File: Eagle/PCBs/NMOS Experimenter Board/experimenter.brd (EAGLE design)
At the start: 83.8 x 99.1 mm, 1526 parts, among them Q100 2N7002, Q101 2N7002, Q102 2N7002, Q103 2N7002, Q104 2N7002, Q105 2N7002, Q106 2N7002, Q107 2N7002, Q108 2N7002, Q109 2N7002, Q110 2N7002, Q111 2N7002, Q112 2N7002, Q113 2N7002, Q114 2N7002, Q115 2N7002, Q116 2N7002, Q117 2N7002, Q118 2N7002, Q119 2N7002, Q120 2N7002, Q2 2N7002, Q25 2N7002, Q26 2N7002, Q27 2N7002, Q28 2N7002, Q29 2N7002, Q3 2N7002, Q30 2N7002, Q31 2N7002, Q32 2N7002, Q33 2N7002, Q34 2N7002, Q35 2N7002, Q36 2N7002, Q37 2N7002, Q38 2N7002, Q39 2N7002, Q4 2N7002, Q40 2N7002, Q41 2N7002, Q42 2N7002, Q43 2N7002, Q44 2N7002, Q45 2N7002, Q46 2N7002, Q47 2N7002, Q48 2N7002, Q49 2N7002, Q5 2N7002, Q50 2N7002, Q51 2N7002, Q52 2N7002, Q53 2N7002, Q54 2N7002, Q55 2N7002, Q56 2N7002, Q57 2N7002, Q58 2N7002, Q59 2N7002, Q6 2N7002, Q60 2N7002, Q61 2N7002, Q62 2N7002, Q63 2N7002, Q64 2N7002, Q65 2N7002, Q66 2N7002, Q67 2N7002, Q68 2N7002, Q69 2N7002, Q7 2N7002, Q70 2N7002, Q71 2N7002, Q72 2N7002, Q73 2N7002, Q74 2N7002, Q75 2N7002, Q76 2N7002, Q77 2N7002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

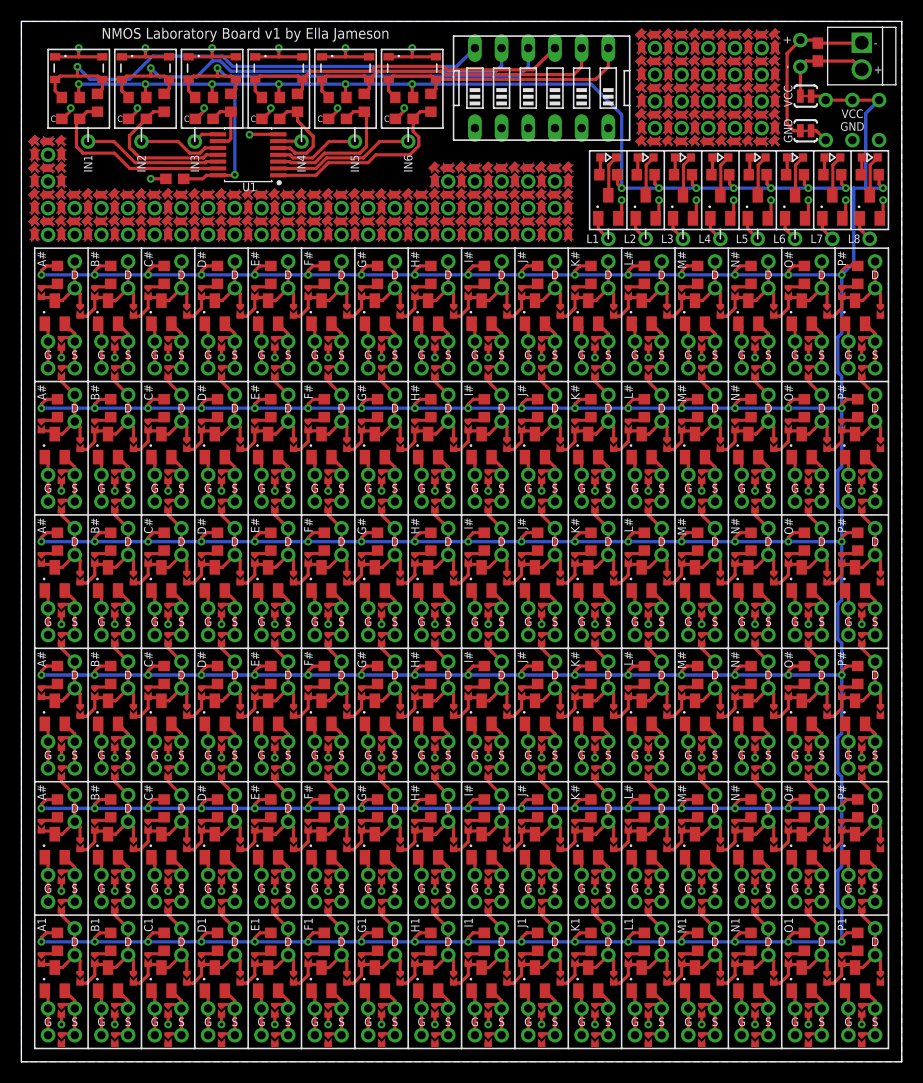
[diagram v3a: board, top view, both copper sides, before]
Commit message: Better power distribution
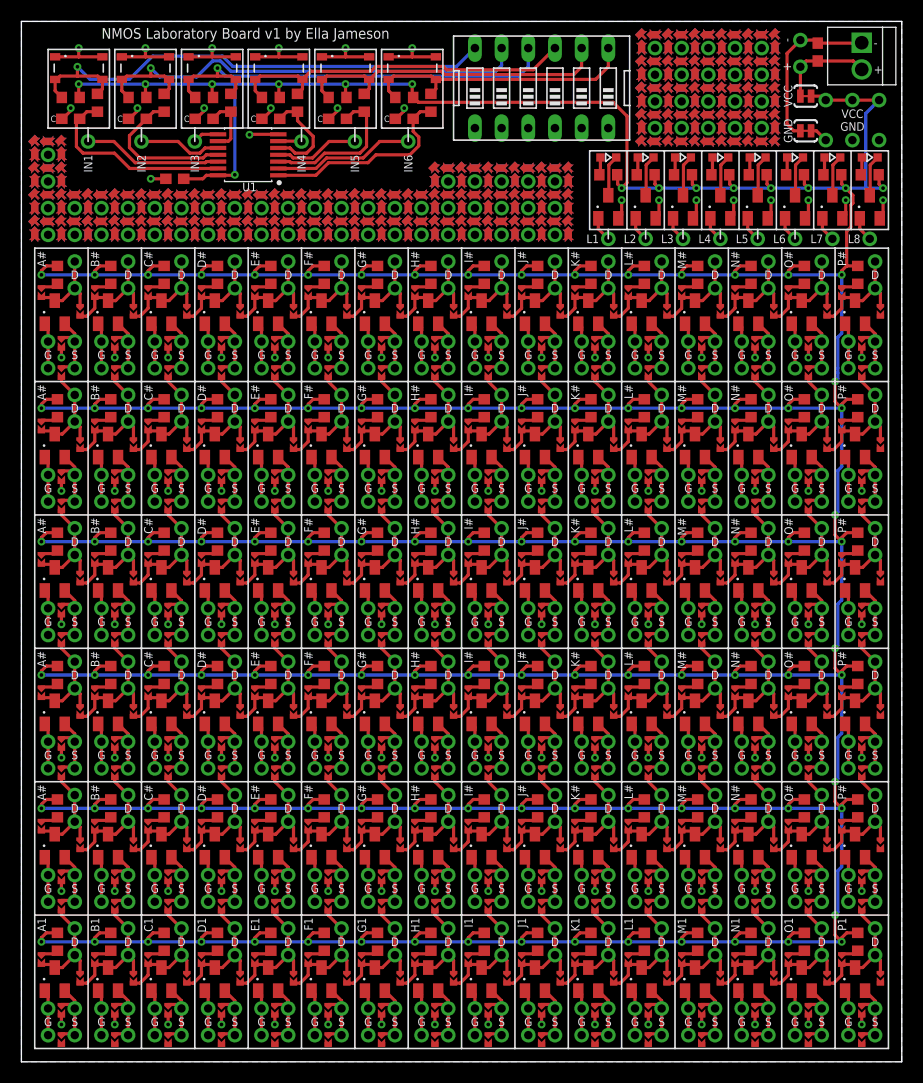
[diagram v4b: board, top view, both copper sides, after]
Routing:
- net VCC: track 865.9 -> 866.2 mm, vias 111 -> 116
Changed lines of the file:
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@@
 </layers>
 <board>
-<fusionsync huburn="a.cGVyc29uYWw6dWUyZGY0M2Ex" projecturn="a.cGVyc29uYWw6dWUyZGY0M2ExIzIwMjMwNDIzNjMzMDQzOTMx" f3durn="urn:adsk.wipprod:dm.lineage:ybcwFhw2S7Sfdtd4-gzlww" pcbguid="" lastpulledtime="" lastsyncedchangeguid="" latestrevisionid="4c6d49ad-edb9-4e4f-9984-d8b9bafc7986" lastsyncedrevisionid="4c6d49ad-edb9-4e4f-9984-d8b9bafc7986" lastboardhashguid="abee2c2b-f349-8aa8-6e4e-c1a4cd3a7c9b" lastpushedtime="2023-04-24T13:14:28Z" linktopcb3d="true"/>
+<fusionsync huburn="a.cGVyc29uYWw6dWUyZGY0M2Ex" projecturn="a.cGVyc29uYWw6dWUyZGY0M2ExIzIwMjMwNDIzNjMzMDQzOTMx" f3durn="urn:adsk.wipprod:dm.lineage:ybcwFhw2S7Sfdtd4-gzlww" pcbguid="" lastpulledtime="" lastsyncedchangeguid="" latestrevisionid="3875195e-3424-4794-8c10-2886cad81166" lastsyncedrevisionid="3875195e-3424-4794-8c10-2886cad81166" lastboardhashguid="f8ce822e-dda0-ce56-7e43-09ef14dc52af" lastpushedtime="2023-04-25T14:47:37Z" linktopcb3d="true"/>
 <plain>
 <wire x1="0" y1="0" x2="0" y2="99.06" width="0.0762" layer="20"/>
@@
 <text x="21.336" y="98.425" size="1.016" layer="22" rot="MR0" align="top-center">NMOS Laboratory Board v1 by Ella Jameson</text>
 <text x="21.336" y="98.425" size="1.016" layer="21" align="top-center">NMOS Laboratory Board v1 by Ella Jameson</text>
-<text x="73.279" y="94.742" size="0.8128" layer="21" rot="R90" align="bottom-center">-</text>
-<text x="73.279" y="97.282" size="0.8128" layer="21" rot="R90" align="bottom-center">+</text>
-<text x="73.279" y="94.742" size="0.8128" layer="22" rot="R90" align="bottom-center">-</text>
-<text x="73.279" y="97.282" size="0.8128" layer="22" rot="R90" align="bottom-center">+</text>
+<text x="73.279" y="97.282" size="0.8128" layer="21" rot="R90" align="bottom-center">-</text>
+<text x="73.279" y="94.742" size="0.8128" layer="21" rot="R90" align="bottom-center">+</text>
+<text x="73.279" y="97.282" size="0.8128" layer="22" rot="R90" align="bottom-center">-</text>
+<text x="73.279" y="94.742" size="0.8128" layer="22" rot="R90" align="bottom-center">+</text>
 <wire x1="57.658" y1="79.248" x2="55.88" y2="79.248" width="0.1524" layer="21"/>
 <wire x1="55.88" y1="79.248" x2="54.102" y2="79.248" width="0.1524" layer="21"/>
@@
 <wire x1="20.32" y1="93.091" x2="24.511" y2="93.091" width="0.3048" layer="16"/>
 <wire x1="24.511" y1="93.091" x2="30.861" y2="93.091" width="0.3048" layer="16"/>
-<wire x1="30.861" y1="93.091" x2="36.83" y2="93.091" width="0.3048" layer="16"/>
+<wire x1="30.861" y1="93.091" x2="37.211" y2="93.091" width="0.3048" layer="16"/>
 <contactref element="C1" pad="1"/>
-<wire x1="36.83" y1="93.091" x2="37.211" y2="93.091" width="0.3048" layer="16"/>
 <wire x1="18.7183" y1="84.41" x2="17.608" y2="84.41" width="0.3048" layer="1"/>
 <wire x1="17.272" y1="84.074" x2="15.455" y2="84.074" width="0.3048" layer="1"/>
@@
 <via x="82.042" y="83.185" extent="1-16" drill="0.35"/>
 <wire x1="74.93" y1="83.185" x2="78.486" y2="83.185" width="0.3048" layer="16"/>
-<wire x1="78.486" y1="83.185" x2="79.248" y2="83.185" width="0.3048" layer="16"/>
 <contactref element="R41" pad="2"/>
-<wire x1="79.248" y1="83.185" x2="80.391" y2="83.185" width="0.3048" layer="16"/>
+<wire x1="78.486" y1="83.185" x2="80.391" y2="83.185" width="0.3048" layer="16"/>
 <wire x1="80.391" y1="83.185" x2="82.042" y2="83.185" width="0.3048" layer="16"/>
 <wire x1="3.429" y1="12.28" x2="2.374" y2="12.28" width="0.3048" layer="1"/>
@@
 <wire x1="73.025" y1="74.93" x2="78.105" y2="74.93" width="0.3048" layer="16"/>
 <wire x1="62.865" y1="74.93" x2="57.785" y2="74.93" width="0.3048" layer="16"/>
-<wire x1="78.105" y1="11.43" x2="78.105" y2="14.45399375" width="0.3048" layer="16"/>
-<wire x1="78.105" y1="14.45399375" x2="77.7352" y2="14.82379375" width="0.3048" layer="16"/>
 <wire x1="77.7352" y1="18.19620625" x2="78.105" y2="18.56600625" width="0.3048" layer="16"/>
 <wire x1="78.105" y1="18.56600625" x2="78.105" y2="24.13" width="0.3048" layer="16"/>
-<wire x1="77.7352" y1="14.82379375" x2="77.7352" y2="18.19620625" width="0.3048" layer="16"/>
-<wire x1="78.105" y1="24.13" x2="78.105" y2="27.15399375" width="0.3048" layer="16"/>
-<wire x1="78.105" y1="27.15399375" x2="77.7352" y2="27.52379375" width="0.3048" layer="16"/>
+<wire x1="77.7352" y1="14.2352" x2="77.7352" y2="18.19620625" width="0.3048" layer="16"/>
 <wire x1="77.7352" y1="30.89620625" x2="78.105" y2="31.26600625" width="0.3048" layer="16"/>
 <wire x1="78.105" y1="31.26600625" x2="78.105" y2="36.83" width="0.3048" layer="16"/>
-<wire x1="77.7352" y1="27.52379375" x2="77.7352" y2="30.89620625" width="0.3048" layer="16"/>
-<wire x1="78.105" y1="36.83" x2="78.105" y2="39.85399375" width="0.3048" layer="16"/>
-<wire x1="78.105" y1="39.85399375" x2="77.7352" y2="40.22379375" width="0.3048" layer="16"/>
+<wire x1="77.7352" y1="26.9352" x2="77.7352" y2="30.89620625" width="0.3048" layer="16"/>
 <wire x1="77.7352" y1="43.59620625" x2="78.105" y2="43.96600625" width="0.3048" layer="16"/>
 <wire x1="78.105" y1="43.96600625" x2="78.105" y2="49.53" width="0.3048" layer="16"/>
-<wire x1="77.7352" y1="40.22379375" x2="77.7352" y2="43.59620625" width="0.3048" layer="16"/>
-<wire x1="78.105" y1="49.53" x2="78.105" y2="52.55399375" width="0.3048" layer="16"/>
-<wire x1="78.105" y1="52.55399375" x2="77.7352" y2="52.92379375" width="0.3048" layer="16"/>
-<wire x1="77.7352" y1="56.29620625" x2="78.105" y2="56.66600625" width="0.3048" layer="16"/>
+<wire x1="77.7352" y1="39.6352" x2="77.7352" y2="43.59620625" width="0.3048" layer="16"/>
+<wire x1="78.105" y1="56.66600625" x2="77.7352" y2="56.29620625" width="0.3048" layer="16"/>
 <wire x1="78.105" y1="56.66600625" x2="78.105" y2="62.23" width="0.3048" layer="16"/>
-<wire x1="77.7352" y1="52.92379375" x2="77.7352" y2="56.29620625" width="0.3048" layer="16"/>
-<wire x1="78.105" y1="62.23" x2="78.105" y2="65.25399375" width="0.3048" layer="16"/>
-<wire x1="78.105" y1="65.25399375" x2="77.7352" y2="65.62379375" width="0.3048" layer="16"/>
 <wire x1="77.7352" y1="68.99620625" x2="78.105" y2="69.36600625" width="0.3048" layer="16"/>
 <wire x1="78.105" y1="69.36600625" x2="78.105" y2="74.93" width="0.3048" layer="16"/>
-<wire x1="77.7352" y1="65.62379375" x2="77.7352" y2="68.99620625" width="0.3048" layer="16"/>
+<wire x1="77.7352" y1="65.62379375" x2="77.7352" y2="66.04" width="0.3048" layer="16"/>
+<wire x1="77.7352" y1="66.04" x2="77.7352" y2="68.99620625" width="0.3048" layer="16"/>
 <wire x1="81.661" y1="91.567" x2="80.391" y2="90.297" width="0.3048" layer="16"/>
 <wire x1="80.391" y1="90.297" x2="80.391" y2="83.185" width="0.3048" layer="16"/>
-<wire x1="78.105" y1="74.93" x2="79.248" y2="76.073" width="0.3048" layer="16"/>
-<wire x1="79.248" y1="76.073" x2="79.248" y2="83.185" width="0.3048" layer="16"/>
-<wire x1="57.15" y1="83.185" x2="57.15" y2="90.17" width="0.3048" layer="16"/>
-<wire x1="54.229" y1="93.091" x2="37.211" y2="93.091" width="0.3048" layer="16"/>
-<wire x1="57.15" y1="90.17" x2="54.229" y2="93.091" width="0.3048" layer="16"/>
+<wire x1="37.299" y1="91.821" x2="37.34195" y2="91.821" width="0.3048" layer="1"/>
+<wire x1="37.34195" y1="91.821" x2="37.80475" y2="91.3582" width="0.3048" layer="1"/>
+<wire x1="37.80475" y1="91.3582" x2="56.3428" y2="91.3582" width="0.3048" layer="1"/>
+<wire x1="57.658" y1="83.693" x2="57.15" y2="83.185" width="0.3048" layer="1"/>
+<wire x1="56.3428" y1="91.3582" x2="57.658" y2="90.043" width="0.3048" layer="1"/>
+<wire x1="57.658" y1="90.043" x2="57.658" y2="83.693" width="0.3048" layer="1"/>
+<wire x1="78.574" y1="79.08395" x2="78.574" y2="75.78" width="0.3048" layer="1"/>
+<wire x1="78.9708" y1="79.48075" x2="78.574" y2="79.08395" width="0.3048" layer="1"/>
+<wire x1="79.169" y1="81.7590875" x2="78.9708" y2="81.5608875" width="0.3048" layer="1"/>
+<wire x1="78.9708" y1="81.5608875" x2="78.9708" y2="79.48075" width="0.3048" layer="1"/>
+<wire x1="78.486" y1="83.185" x2="79.169" y2="82.502" width="0.3048" layer="1"/>
+<wire x1="79.169" y1="82.502" x2="79.169" y2="81.7590875" width="0.3048" layer="1"/>
+<wire x1="77.7352" y1="14.2352" x2="77.47" y2="13.97" width="0.3048" layer="16"/>
+<via x="77.47" y="13.97" extent="1-16" drill="0.35"/>
+<wire x1="77.47" y1="13.97" x2="77.47" y2="12.065" width="0.3048" layer="1"/>
+<wire x1="77.47" y1="12.065" x2="78.105" y2="11.43" width="0.3048" layer="1"/>
+<wire x1="77.7352" y1="26.9352" x2="77.47" y2="26.67" width="0.3048" layer="16"/>
+<via x="77.47" y="26.67" extent="1-16" drill="0.35"/>
+<wire x1="77.47" y1="26.67" x2="77.47" y2="24.765" width="0.3048" layer="1"/>
+<wire x1="77.47" y1="24.765" x2="78.105" y2="24.13" width="0.3048" layer="1"/>
+<wire x1="77.7352" y1="39.6352" x2="77.47" y2="39.37" width="0.3048" layer="16"/>
+<via x="77.47" y="39.37" extent="1-16" drill="0.35"/>
+<wire x1="77.47" y1="39.37" x2="77.47" y2="37.465" width="0.3048" layer="1"/>
+<wire x1="77.47" y1="37.465" x2="78.105" y2="36.83" width="0.3048" layer="1"/>
+<wire x1="77.7352" y1="52.3352" x2="77.47" y2="52.07" width="0.3048" layer="16"/>
+<via x="77.47" y="52.07" extent="1-16" drill="0.35"/>
+<wire x1="77.47" y1="52.07" x2="77.47" y2="50.165" width="0.3048" layer="1"/>
+<wire x1="77.47" y1="50.165" x2="78.105" y2="49.53" width="0.3048" layer="1"/>
+<wire x1="77.7352" y1="56.29620625" x2="77.7352" y2="52.3352" width="0.3048" layer="16"/>
+<wire x1="77.7352" y1="65.62379375" x2="77.7352" y2="65.0352" width="0.3048" layer="16"/>
+<wire x1="77.7352" y1="65.0352" x2="77.47" y2="64.77" width="0.3048" layer="16"/>
+<via x="77.47" y="64.77" extent="1-16" drill="0.35"/>
+<wire x1="77.47" y1="64.77" x2="77.47" y2="62.865" width="0.3048" layer="1"/>
+<wire x1="77.47" y1="62.865" x2="78.105" y2="62.23" width="0.3048" layer="1"/>
 </signal>
 <signal name="N$8">

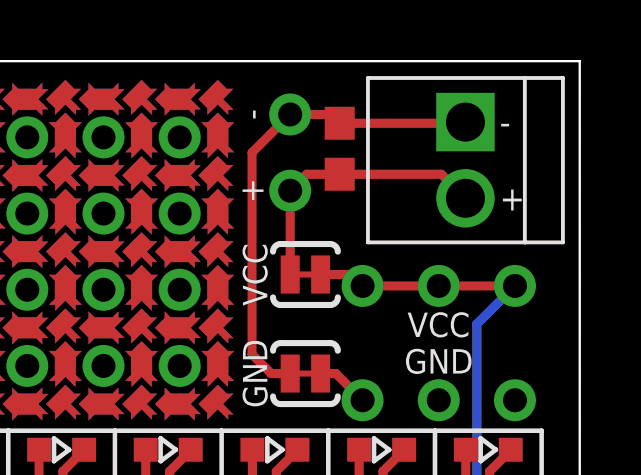
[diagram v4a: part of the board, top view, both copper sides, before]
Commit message: Fixed power input connector
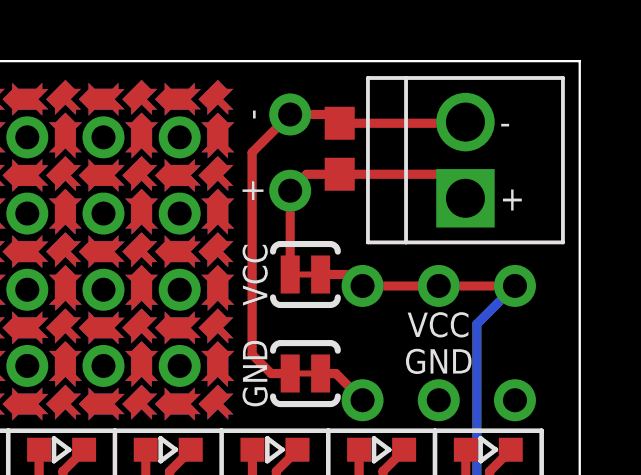
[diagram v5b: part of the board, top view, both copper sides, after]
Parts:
- turned J1 to 90 degrees
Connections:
- net N$321: now also J1.P$2; no longer J1.P$1
- net N$322: now also J1.P$1; no longer J1.P$2
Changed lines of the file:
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@@
 </layers>
 <board>
-<fusionsync huburn="a.cGVyc29uYWw6dWUyZGY0M2Ex" projecturn="a.cGVyc29uYWw6dWUyZGY0M2ExIzIwMjMwNDIzNjMzMDQzOTMx" f3durn="urn:adsk.wipprod:dm.lineage:ybcwFhw2S7Sfdtd4-gzlww" pcbguid="" lastpulledtime="" lastsyncedchangeguid="" latestrevisionid="3875195e-3424-4794-8c10-2886cad81166" lastsyncedrevisionid="3875195e-3424-4794-8c10-2886cad81166" lastboardhashguid="f8ce822e-dda0-ce56-7e43-09ef14dc52af" lastpushedtime="2023-04-25T14:47:37Z" linktopcb3d="true"/>
+<fusionsync huburn="a.cGVyc29uYWw6dWUyZGY0M2Ex" projecturn="a.cGVyc29uYWw6dWUyZGY0M2ExIzIwMjMwNDIzNjMzMDQzOTMx" f3durn="urn:adsk.wipprod:dm.lineage:ybcwFhw2S7Sfdtd4-gzlww" pcbguid="" lastpulledtime="" lastsyncedchangeguid="" latestrevisionid="b5bfb191-6589-4ccd-a022-24fec571c67f" lastsyncedrevisionid="b5bfb191-6589-4ccd-a022-24fec571c67f" lastboardhashguid="9ff4f2cc-dc7f-5f8a-e66d-b9aa640ada64" lastpushedtime="2023-04-25T14:52:07Z" linktopcb3d="true"/>
 <plain>
 <wire x1="0" y1="0" x2="0" y2="99.06" width="0.0762" layer="20"/>
@@
 <element name="B5" library="ellajameson-core" library_urn="urn:adsk.eagle:library:3740209" package="PROTOPAD-THT-PAD" package3d_urn="urn:adsk.eagle:package:40167003/2" value="TPTHT" x="31.75" y="87.63" smashed="yes"/>
 <element name="B6" library="ellajameson-core" library_urn="urn:adsk.eagle:library:3740209" package="PROTOPAD-THT-PAD" package3d_urn="urn:adsk.eagle:package:40167003/2" value="TPTHT" x="36.83" y="87.63" smashed="yes"/>
-<element name="J1" library="ellajameson-core" library_urn="urn:adsk.eagle:library:3740209" package="OSTVN02A150" package3d_urn="urn:adsk.eagle:package:12594929/5" value="" x="80.01" y="95.758" smashed="yes" rot="R270"/>
+<element name="J1" library="ellajameson-core" library_urn="urn:adsk.eagle:library:3740209" package="OSTVN02A150" package3d_urn="urn:adsk.eagle:package:12594929/5" value="" x="80.01" y="95.758" smashed="yes" rot="R90"/>
 <element name="C1" library="ellajameson-core" library_urn="urn:adsk.eagle:library:3740209" package="C0603" package3d_urn="urn:adsk.eagle:package:7587834/2" value="0.1u" x="14.605" y="84.074" smashed="yes" rot="R180"/>
 <element name="C4" library="ellajameson-core" library_urn="urn:adsk.eagle:library:3740209" package="C0603" package3d_urn="urn:adsk.eagle:package:7587834/2" value="0.1u" x="75.819" y="96.139" smashed="yes" rot="R270"/>
@@
 </signal>
 <signal name="N$321">
-<contactref element="J1" pad="P$1"/>
 <contactref element="C4" pad="1"/>
 <contactref element="VIN-1" pad="P1"/>
 <contactref element="SJ2" pad="1"/>
-<wire x1="80.01" y1="97.028" x2="79.971" y2="96.989" width="0.3048" layer="1"/>
-<wire x1="79.971" y1="96.989" x2="75.819" y2="96.989" width="0.3048" layer="1"/>
 <wire x1="74.168" y1="97.282" x2="75.526" y2="97.282" width="0.3048" layer="1"/>
 <wire x1="75.526" y1="97.282" x2="75.819" y2="96.989" width="0.3048" layer="1"/>
@@
 <wire x1="73.533" y1="88.646" x2="72.898" y2="89.281" width="0.3048" layer="1"/>
 <wire x1="72.898" y1="89.281" x2="72.898" y2="96.012" width="0.3048" layer="1"/>
+<contactref element="J1" pad="P$2"/>
+<wire x1="75.819" y1="96.989" x2="79.971" y2="96.989" width="0.3048" layer="1"/>
+<wire x1="79.971" y1="96.989" x2="80.01" y2="97.028" width="0.3048" layer="1"/>
 </signal>
 <signal name="N$322">
 <contactref element="VIN+1" pad="P1"/>
-<contactref element="J1" pad="P$2"/>
 <contactref element="C4" pad="2"/>
 <contactref element="SJ1" pad="1"/>
-<wire x1="80.01" y1="94.488" x2="79.209" y2="95.289" width="0.3048" layer="1"/>
-<wire x1="79.209" y1="95.289" x2="75.819" y2="95.289" width="0.3048" layer="1"/>
 <wire x1="74.168" y1="94.742" x2="74.715" y2="95.289" width="0.3048" layer="1"/>
 <wire x1="74.715" y1="95.289" x2="75.819" y2="95.289" width="0.3048" layer="1"/>
 <wire x1="74.168" y1="91.948" x2="74.168" y2="94.742" width="0.3048" layer="1"/>
+<contactref element="J1" pad="P$1"/>
+<wire x1="75.819" y1="95.289" x2="79.209" y2="95.289" width="0.3048" layer="1"/>
+<wire x1="79.209" y1="95.289" x2="80.01" y2="94.488" width="0.3048" layer="1"/>
 </signal>
 <signal name="N$4">
